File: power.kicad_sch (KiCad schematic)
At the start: 1 part, among them IC2 TPS23734RMTR

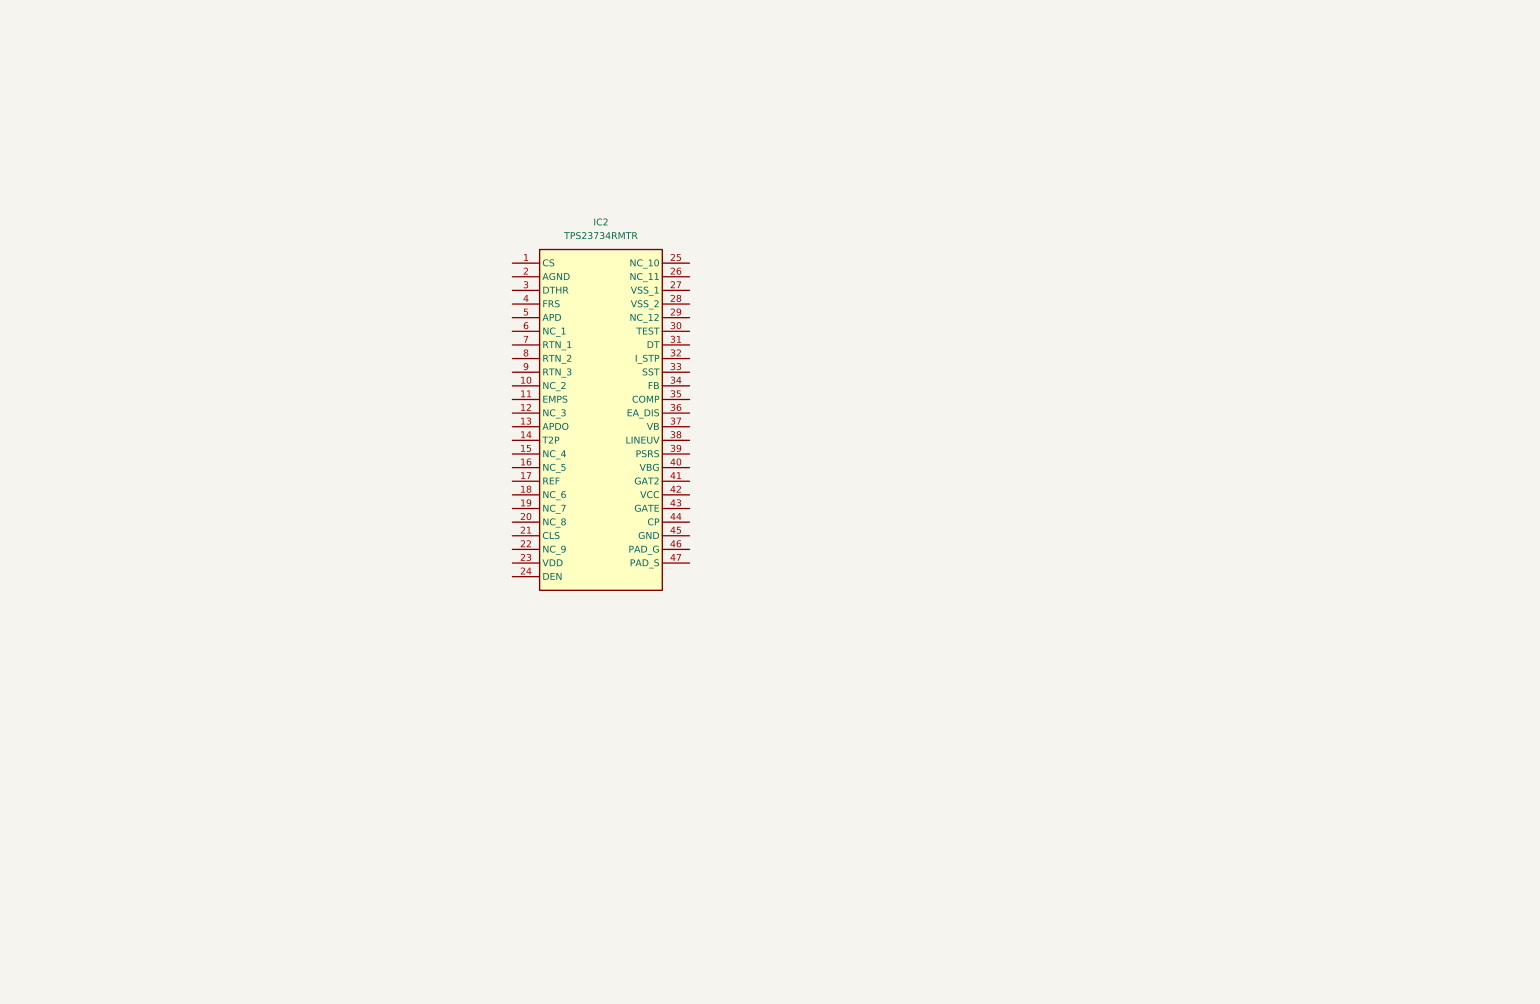
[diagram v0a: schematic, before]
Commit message: Update schematic power symbols and add backups
Replaced +48V and -48V power symbols with VDD and VSS in peripherals.kicad_sch, updated title blocks and paper sizes in all .kicad_sch files, and added new schematic symbols for test points, capacitors, resistors, MOSFET, and optocoupler in power.kicad_sch. Added multiple new backup ZIP files for POETempSensor.
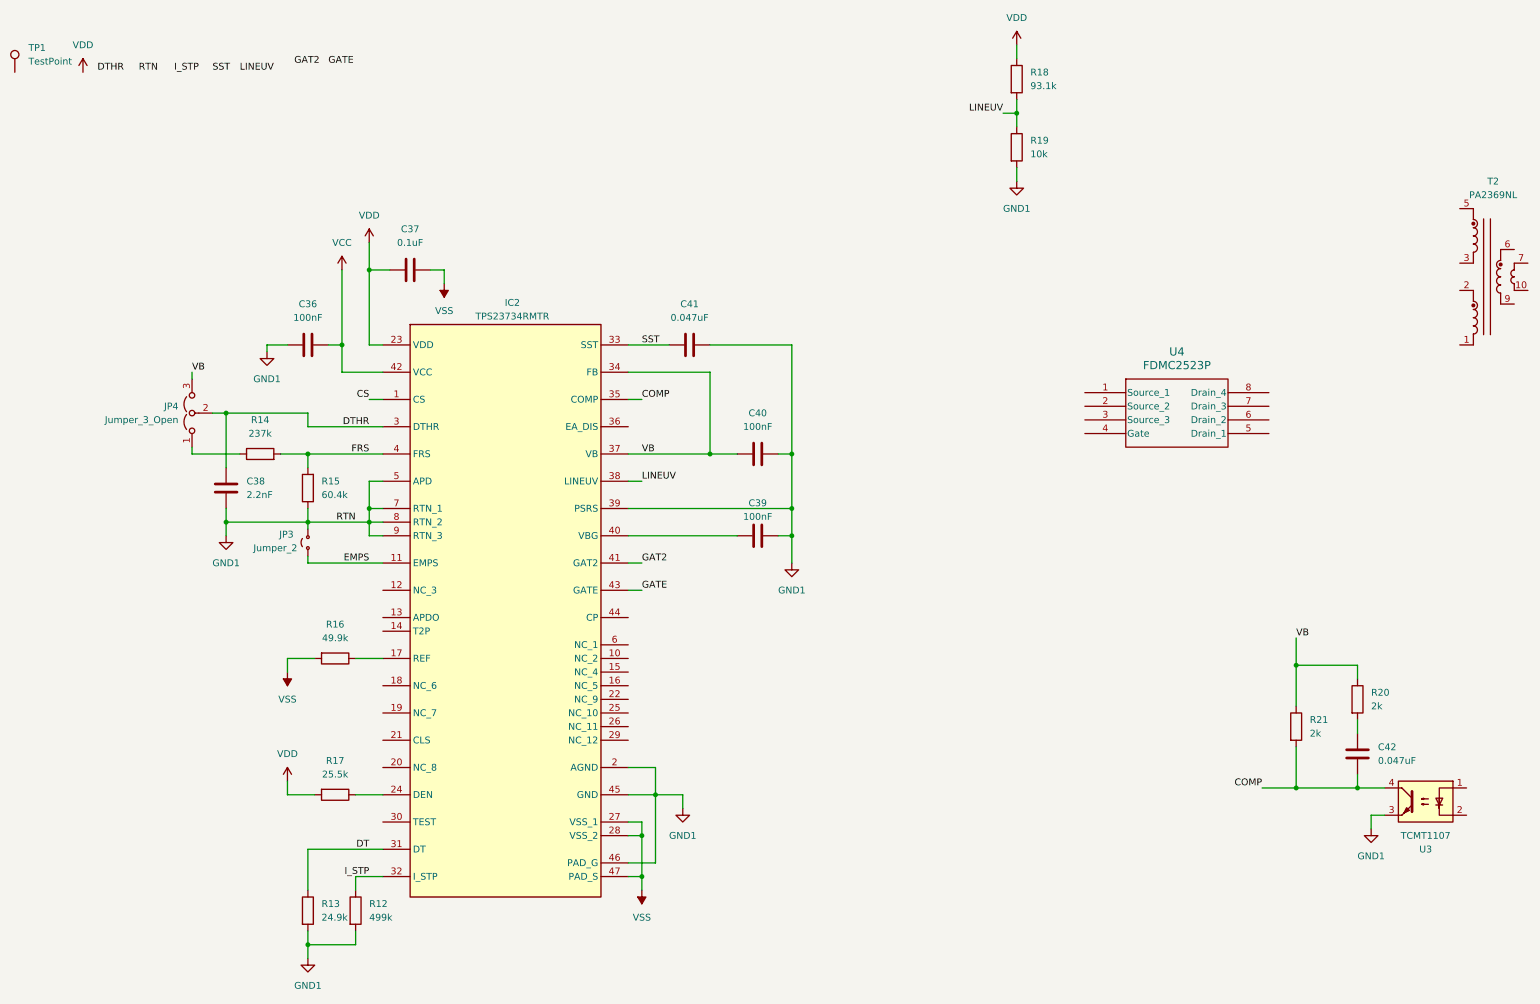
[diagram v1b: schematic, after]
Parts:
- added C36, C39, C40: 100nF, symbol Device:C
- added C37: 0.1uF, symbol Device:C
- added C38: 2.2nF, symbol Device:C
- added C41, C42: 0.047uF, symbol Device:C
- added JP3: Jumper_2, symbol Jumper:Jumper_2_Small_Open
- added JP4: Jumper_3_Open, symbol Jumper:Jumper_3_Open
- added R12: 499k, symbol Device:R
- added R13: 24.9k, symbol Device:R
- added R14: 237k, symbol Device:R
- added R15: 60.4k, symbol Device:R
- added R16: 49.9k, symbol Device:R
- added R17: 25.5k, symbol Device:R
- added R18: 93.1k, symbol Device:R
- added R19: 10k, symbol Device:R
- added R20, R21: 2k, symbol Device:R
- added T2: PA2369NL, SamacSys_Parts:PA2369NL, symbol MyLibrary:PA2369NL
- added TP1: TestPoint, symbol Connector:TestPoint
- added U3: TCMT1107, Package_SO:SOP-4_4.4x2.6mm_P1.27mm, symbol Isolator:TCMT1107
- added U4: FDMC2523P, FDMC_2523P_ONS, symbol FDMC2523P:FDMC2523P
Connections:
- net CS: now reaches IC2.1 (CS)
- net EMPS: now reaches IC2.11 (EMPS)
- net EMPS: now also JP3.1 (A)
- net at IC2.17 (REF): now also R16.1
- net GND1: now reaches IC2.2 (AGND)
- net GND1: now also IC2.39 (PSRS), IC2.45 (GND), IC2.46 (PAD_G), IC2.5 (APD), IC2.7 (RTN_1), IC2.8 (RTN_2), IC2.9 (RTN_3), C36.1, C38.1, C39.2, C40.2, C41.2, JP3.2 (B), R12.2, R13.2, R15.1, R19.2, U3.3
- net VDD: now reaches IC2.23 (VDD)
- net VDD: now also C37.1, R17.2, R18.1
- net at IC2.24 (DEN): now also R17.1
- net VSS: now reaches IC2.27 (VSS_1)
- net VSS: now also IC2.28 (VSS_2), IC2.47 (PAD_S), C37.2, R16.2
- net DTHR: now reaches IC2.3 (DTHR)
- net DTHR: now also C38.2, JP4.2 (C)
- net DT: now reaches IC2.31 (DT)
- net DT: now also R13.1
- net I_STP: now reaches IC2.32 (I_STP)
- net I_STP: now also R12.1
- net SST: now reaches IC2.33 (SST)
- net SST: now also C41.1
- net VB: now reaches IC2.34 (FB)
- net VB: now also IC2.37 (VB), C40.1, JP4.3 (B), R20.1, R21.1
- net COMP: now reaches IC2.35 (COMP)
- net COMP: now also C42.2, R21.2, U3.4
- net LINEUV: now reaches IC2.38 (LINEUV)
- net LINEUV: now also R18.2, R19.1
- net FRS: now reaches IC2.4 (FRS)
- net FRS: now also R14.2, R15.2
- net at IC2.40 (VBG): now also C39.1
- net GAT2: now reaches IC2.41 (GAT2)
- net VCC: now reaches IC2.42 (VCC)
- net VCC: now also C36.2
- net GATE: now reaches IC2.43 (GATE)
- new net: C42.1, R20.2
- new net: JP4.1 (A), R14.1
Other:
- title: (none) -> Power Management
- moved on the sheet: IC2
